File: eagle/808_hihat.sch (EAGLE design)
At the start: 129 parts, among them IC1 TL072P, IC2 TL072P, U4 4584N

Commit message: redoing board by hand from schematic
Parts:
- removed TM1*1, TM2*1: 220KB, TR808clone:TRIM_EU-CT6
- R44*1: value 150K -> 300K
- R45*1: value 100K -> 270K
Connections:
- removed net N$10: C5*1.2, TM2*1.E, U4E.I
- removed net N$11: C6*1.2, TM1*1.E, U4F.I
- net N$15: now also C5*1.2, U4E.I; no longer TM2*1.S
- net N$16: now also C6*1.2, U4F.I; no longer TM1*1.S
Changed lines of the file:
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@@
 <part name="R42*1" library="TR808clone" deviceset="R-EU_" device="0207/5V" value="680K"/>
 <part name="R43*1" library="TR808clone" deviceset="R-EU_" device="0207/5V" value="220K"/>
-<part name="R45*1" library="TR808clone" deviceset="R-EU_" device="0207/5V" value="100K"/>
+<part name="R45*1" library="TR808clone" deviceset="R-EU_" device="0207/5V" value="270K"/>
 <part name="C1*1" library="TR808clone" deviceset="C-EU" device="4MM_PITCH" value="18n"/>
 <part name="C2*1" library="TR808clone" deviceset="C-EU" device="3.5MM_PITCH" value="10n"/>
@@
 <part name="V9" library="supply1" deviceset="GND" device=""/>
 <part name="V10" library="supply1" deviceset="GND" device=""/>
-<part name="TM2*1" library="TR808clone" deviceset="TRIM_EU-" device="CT6" value="220KB"/>
-<part name="TM1*1" library="TR808clone" deviceset="TRIM_EU-" device="CT6" value="220KB"/>
-<part name="R44*1" library="TR808clone" deviceset="R-EU_" device="0207/5V" value="150K"/>
+<part name="R44*1" library="TR808clone" deviceset="R-EU_" device="0207/5V" value="300K"/>
 <part name="V11" library="supply1" deviceset="GND" device=""/>
 <part name="IC1" library="linear" deviceset="TL072" device="P"/>
@@
 <instance part="V9" gate="1" x="-55.88" y="-40.64"/>
 <instance part="V10" gate="1" x="-55.88" y="-12.7"/>
-<instance part="TM2*1" gate="1" x="-50.8" y="-22.86" smashed="yes" rot="R90">
-<attribute name="NAME" x="-57.15" y="-18.669" size="1.778" layer="95" rot="R180"/>
-<attribute name="VALUE" x="-57.15" y="-21.59" size="1.778" layer="96" rot="R180"/>
-</instance>
-<instance part="TM1*1" gate="1" x="-53.34" y="7.62" smashed="yes" rot="R90">
-<attribute name="NAME" x="-59.69" y="11.811" size="1.778" layer="95" rot="R180"/>
-<attribute name="VALUE" x="-59.69" y="8.89" size="1.778" layer="96" rot="R180"/>
-</instance>
 <instance part="R44*1" gate="G$1" x="-40.64" y="12.7" smashed="yes" rot="MR180">
 <attribute name="NAME" x="-44.45" y="11.2014" size="1.778" layer="95" rot="MR180"/>
@@
 </segment>
 </net>
-<net name="N$10" class="0">
-<segment>
-<pinref part="U4" gate="E" pin="I"/>
-<pinref part="C5*1" gate="G$1" pin="2"/>
-<wire x1="-55.88" y1="-30.48" x2="-55.88" y2="-22.86" width="0.1524" layer="91"/>
-<pinref part="TM2*1" gate="1" pin="E"/>
-<junction x="-55.88" y="-30.48"/>
-</segment>
-</net>
-<net name="N$11" class="0">
-<segment>
-<pinref part="U4" gate="F" pin="I"/>
-<pinref part="C6*1" gate="G$1" pin="2"/>
-<pinref part="TM1*1" gate="1" pin="E"/>
-<wire x1="-58.42" y1="7.62" x2="-58.42" y2="-2.54" width="0.1524" layer="91"/>
-<wire x1="-58.42" y1="-2.54" x2="-55.88" y2="-2.54" width="0.1524" layer="91"/>
-<junction x="-55.88" y="-2.54"/>
-</segment>
-</net>
 <net name="N$12" class="0">
 <segment>
@@
 <net name="N$15" class="0">
 <segment>
-<pinref part="TM2*1" gate="1" pin="S"/>
 <pinref part="R45*1" gate="G$1" pin="1"/>
-<wire x1="-50.8" y1="-17.78" x2="-45.72" y2="-17.78" width="0.1524" layer="91"/>
+<pinref part="U4" gate="E" pin="I"/>
+<pinref part="C5*1" gate="G$1" pin="2"/>
+<wire x1="-55.88" y1="-30.48" x2="-55.88" y2="-17.78" width="0.1524" layer="91"/>
+<junction x="-55.88" y="-30.48"/>
+<wire x1="-45.72" y1="-17.78" x2="-55.88" y2="-17.78" width="0.1524" layer="91"/>
 </segment>
 </net>
 <net name="N$16" class="0">
 <segment>
-<pinref part="TM1*1" gate="1" pin="S"/>
 <pinref part="R44*1" gate="G$1" pin="1"/>
-<wire x1="-53.34" y1="12.7" x2="-45.72" y2="12.7" width="0.1524" layer="91"/>
-</segment>
-</net>
+<wire x1="-58.42" y1="12.7" x2="-45.72" y2="12.7" width="0.1524" layer="91"/>
+<pinref part="U4" gate="F" pin="I"/>
+<pinref part="C6*1" gate="G$1" pin="2"/>
+<wire x1="-58.42" y1="12.7" x2="-58.42" y2="-2.54" width="0.1524" layer="91"/>
+<wire x1="-58.42" y1="-2.54" x2="-55.88" y2="-2.54" width="0.1524" layer="91"/>
+<junction x="-55.88" y="-2.54"/>
+</segment>
+</net>

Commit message: three routes left
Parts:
- R153*: device TR808clone:R-EU_0207/2V -> rcl:R-US_0207/5V
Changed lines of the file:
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@@
 <part name="C73*" library="TR808clone" deviceset="C-EU" device="3.5MM_PITCH" value="1n"/>
 <part name="R147*" library="TR808clone" deviceset="R-EU_" device="0207/2V" value="2K7"/>
-<part name="R153*" library="TR808clone" deviceset="R-EU_" device="0207/2V" value="2K7"/>
+<part name="R153*" library="rcl" deviceset="R-US_" device="0207/5V" value="2K7"/>
 <part name="R146*" library="TR808clone" deviceset="R-EU_" device="0207/5V" value="68K"/>
 <part name="R155*" library="TR808clone" deviceset="R-EU_" device="0207/5V" value="68K"/>

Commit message: routed but rough
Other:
- note added: "Hi-Hats"
- note removed: "HitHat"
- moved on the sheet: R44*1
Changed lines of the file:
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@@
 <description>HitHat</description>
 <plain>
-<text x="2.54" y="106.68" size="3.81" layer="94">HitHat</text>
+<text x="2.54" y="106.68" size="3.81" layer="94">Hi-Hats</text>
 </plain>
 <instances>
@@
 <instance part="V9" gate="1" x="-55.88" y="-40.64"/>
 <instance part="V10" gate="1" x="-55.88" y="-12.7"/>
-<instance part="R44*1" gate="G$1" x="-40.64" y="12.7" smashed="yes" rot="MR180">
-<attribute name="NAME" x="-44.45" y="11.2014" size="1.778" layer="95" rot="MR180"/>
-<attribute name="VALUE" x="-44.45" y="8.382" size="1.778" layer="96" rot="MR180"/>
+<instance part="R44*1" gate="G$1" x="-40.64" y="15.24" smashed="yes" rot="MR180">
+<attribute name="NAME" x="-44.45" y="13.7414" size="1.778" layer="95" rot="MR180"/>
+<attribute name="VALUE" x="-44.45" y="10.922" size="1.778" layer="96" rot="MR180"/>
 </instance>
 <instance part="V11" gate="1" x="-45.72" y="-12.7"/>
@@
 <instance part="IC1" gate="B" x="147.32" y="7.62" rot="MR180"/>
 <instance part="IC2" gate="A" x="7.62" y="-68.58" rot="MR180"/>
-<instance part="P+3" gate="1" x="-45.72" y="20.32"/>
+<instance part="P+3" gate="1" x="-45.72" y="10.16"/>
 <instance part="CH_ACCENT" gate="1" x="-106.68" y="114.3"/>
 <instance part="CH_TRIG" gate="1" x="-139.7" y="111.76"/>
@@
 <wire x1="-35.56" y1="-2.54" x2="-33.02" y2="-2.54" width="0.1524" layer="91"/>
 <pinref part="R44*1" gate="G$1" pin="2"/>
-<wire x1="-35.56" y1="12.7" x2="-35.56" y2="-2.54" width="0.1524" layer="91"/>
+<wire x1="-35.56" y1="15.24" x2="-35.56" y2="-2.54" width="0.1524" layer="91"/>
 <junction x="-35.56" y="-2.54"/>
 </segment>
@@
 <segment>
 <pinref part="R44*1" gate="G$1" pin="1"/>
-<wire x1="-58.42" y1="12.7" x2="-45.72" y2="12.7" width="0.1524" layer="91"/>
+<wire x1="-58.42" y1="12.7" x2="-45.72" y2="15.24" width="0.1524" layer="91"/>
 <pinref part="U4" gate="F" pin="I"/>
 <pinref part="C6*1" gate="G$1" pin="2"/>
@@
 <segment>
 <pinref part="U4" gate="P" pin="VDD"/>
-<wire x1="-45.72" y1="5.08" x2="-45.72" y2="17.78" width="0.1524" layer="91"/>
+<wire x1="-45.72" y1="5.08" x2="-45.72" y2="7.62" width="0.1524" layer="91"/>
 <pinref part="P+3" gate="1" pin="+5V"/>
 </segment>

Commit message: labeled the transistor values
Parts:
- Q21*, Q22*, Q23*, Q24*, Q26*, Q27*, Q28*, Q29*, Q3*, Q30*, Q31*, Q4*: value (none) -> BC546
- Q7*, Q8*: value (none) -> BC556
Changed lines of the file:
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@@
 </classes>
 <parts>
-<part name="Q4*" library="transistor" deviceset="*-NPN-" device="TO92-CBE" technology="BC546"/>
-<part name="Q8*" library="transistor" deviceset="*-PNP-" device="TO92-EBC" technology="BC556A"/>
+<part name="Q4*" library="transistor" deviceset="*-NPN-" device="TO92-CBE" technology="BC546" value="BC546"/>
+<part name="Q8*" library="transistor" deviceset="*-PNP-" device="TO92-EBC" technology="BC556A" value="BC556"/>
 <part name="R7*" library="TR808clone" deviceset="R-EU_" device="0207/5V" value="10K"/>
 <part name="R11*" library="TR808clone" deviceset="R-EU_" device="0207/5V" value="22K"/>
@@
 <part name="V358" library="supply1" deviceset="GND" device=""/>
 <part name="V359" library="supply1" deviceset="GND" device=""/>
-<part name="Q3*" library="transistor" deviceset="*-NPN-" device="TO92-CBE" technology="BC546"/>
-<part name="Q7*" library="transistor" deviceset="*-PNP-" device="TO92-EBC" technology="BC556A"/>
+<part name="Q3*" library="transistor" deviceset="*-NPN-" device="TO92-CBE" technology="BC546" value="BC546"/>
+<part name="Q7*" library="transistor" deviceset="*-PNP-" device="TO92-EBC" technology="BC556A" value="BC556"/>
 <part name="R8*" library="TR808clone" deviceset="R-EU_" device="0207/5V" value="10K"/>
 <part name="R12*" library="TR808clone" deviceset="R-EU_" device="0207/5V" value="22K"/>
@@
 <part name="V363" library="supply1" deviceset="GND" device=""/>
 <part name="R130*" library="TR808clone" deviceset="R-EU_" device="0207/5V" value="10K"/>
-<part name="Q21*" library="transistor" deviceset="*-NPN-" device="TO92-CBE" technology="BC546"/>
+<part name="Q21*" library="transistor" deviceset="*-NPN-" device="TO92-CBE" technology="BC546" value="BC546"/>
 <part name="V364" library="supply1" deviceset="GND" device=""/>
 <part name="C60*" library="TR808clone" deviceset="CPOL-EU" device="E2.5-5" value="10/16"/>
 <part name="V365" library="supply1" deviceset="GND" device=""/>
 <part name="R133*" library="TR808clone" deviceset="R-EU_" device="0207/5V" value="10K"/>
-<part name="Q22*" library="transistor" deviceset="*-NPN-" device="TO92-CBE" technology="BC546"/>
-<part name="Q23*" library="transistor" deviceset="*-NPN-" device="TO92-CBE" technology="BC546"/>
+<part name="Q22*" library="transistor" deviceset="*-NPN-" device="TO92-CBE" technology="BC546" value="BC546"/>
+<part name="Q23*" library="transistor" deviceset="*-NPN-" device="TO92-CBE" technology="BC546" value="BC546"/>
 <part name="R134*" library="TR808clone" deviceset="R-EU_" device="0207/5V" value="100K"/>
 <part name="R135*" library="TR808clone" deviceset="R-EU_" device="0207/5V" value="10K"/>
-<part name="Q24*" library="transistor" deviceset="*-NPN-" device="TO92-CBE" technology="BC546"/>
+<part name="Q24*" library="transistor" deviceset="*-NPN-" device="TO92-CBE" technology="BC546" value="BC546"/>
 <part name="R137*" library="TR808clone" deviceset="R-EU_" device="0207/5V" value="470R"/>
 <part name="C62*" library="TR808clone" deviceset="CPOL-EU" device="E2.5-5" value=".47/50"/>
@@
 <part name="C61*" library="TR808clone" deviceset="CPOL-EU" device="E2.5-5" value="47/16"/>
 <part name="V370" library="supply1" deviceset="GND" device=""/>
-<part name="Q29*" library="transistor" deviceset="*-NPN-" device="TO92-CBE" technology="BC546"/>
+<part name="Q29*" library="transistor" deviceset="*-NPN-" device="TO92-CBE" technology="BC546" value="BC546"/>
 <part name="R143*" library="TR808clone" deviceset="R-EU_" device="0207/5V" value="33K"/>
 <part name="V371" library="supply1" deviceset="GND" device=""/>
 <part name="R136*" library="TR808clone" deviceset="R-EU_" device="0207/5V" value="100R"/>
-<part name="Q28*" library="transistor" deviceset="*-NPN-" device="TO92-CBE" technology="BC546"/>
+<part name="Q28*" library="transistor" deviceset="*-NPN-" device="TO92-CBE" technology="BC546" value="BC546"/>
 <part name="R141*" library="TR808clone" deviceset="R-EU_" device="0207/5V" value="33K"/>
 <part name="R173*" library="TR808clone" deviceset="R-EU_" device="0207/5V" value="330K"/>
 <part name="C63*" library="TR808clone" deviceset="CPOL-EU" device="E2.5-5" value=".47/50"/>
 <part name="V374" library="supply1" deviceset="GND" device=""/>
-<part name="Q27*" library="transistor" deviceset="*-NPN-" device="TO92-CBE" technology="BC546"/>
+<part name="Q27*" library="transistor" deviceset="*-NPN-" device="TO92-CBE" technology="BC546" value="BC546"/>
 <part name="C67*" library="TR808clone" deviceset="C-EU" device="4MM_PITCH" value="22n"/>
-<part name="Q30*" library="transistor" deviceset="*-NPN-" device="TO92-CBE" technology="BC546"/>
+<part name="Q30*" library="transistor" deviceset="*-NPN-" device="TO92-CBE" technology="BC546" value="BC546"/>
 <part name="V375" library="supply1" deviceset="GND" device=""/>
 <part name="V376" library="supply1" deviceset="GND" device=""/>
@@
 <part name="V383" library="supply1" deviceset="GND" device=""/>
 <part name="V384" library="supply1" deviceset="GND" device=""/>
-<part name="Q26*" library="transistor" deviceset="*-NPN-" device="TO92-CBE" technology="BC546"/>
-<part name="Q31*" library="transistor" deviceset="*-NPN-" device="TO92-CBE" technology="BC546"/>
+<part name="Q26*" library="transistor" deviceset="*-NPN-" device="TO92-CBE" technology="BC546" value="BC546"/>
+<part name="Q31*" library="transistor" deviceset="*-NPN-" device="TO92-CBE" technology="BC546" value="BC546"/>
 <part name="C80*" library="TR808clone" deviceset="C-EU" device="3.5MM_PITCH" value="470p"/>
 <part name="C74*" library="TR808clone" deviceset="C-EU" device="3.5MM_PITCH" value="470p"/>

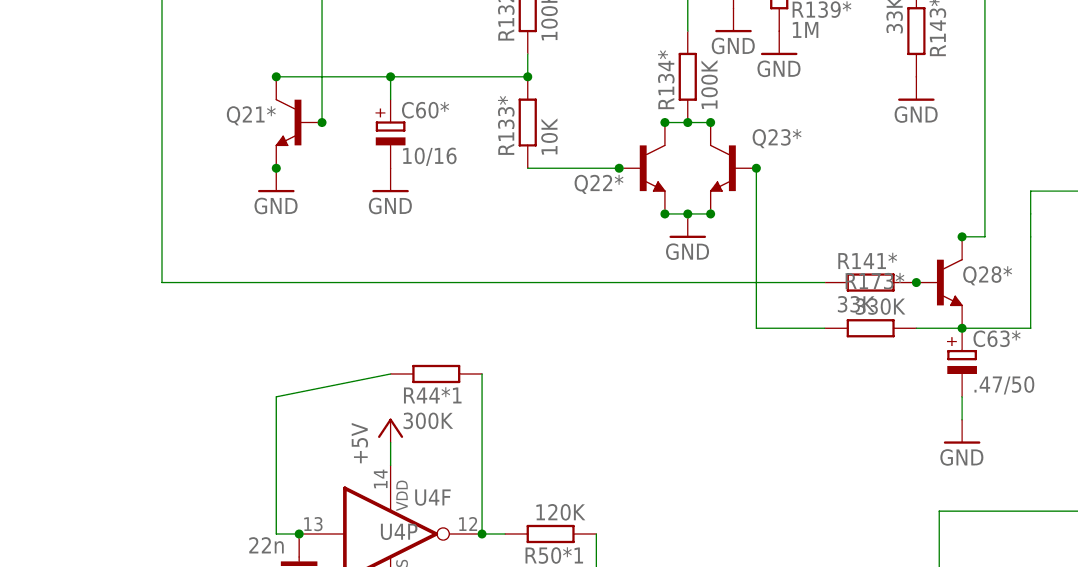
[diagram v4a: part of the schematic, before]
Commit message: ready for a test run on the cnc
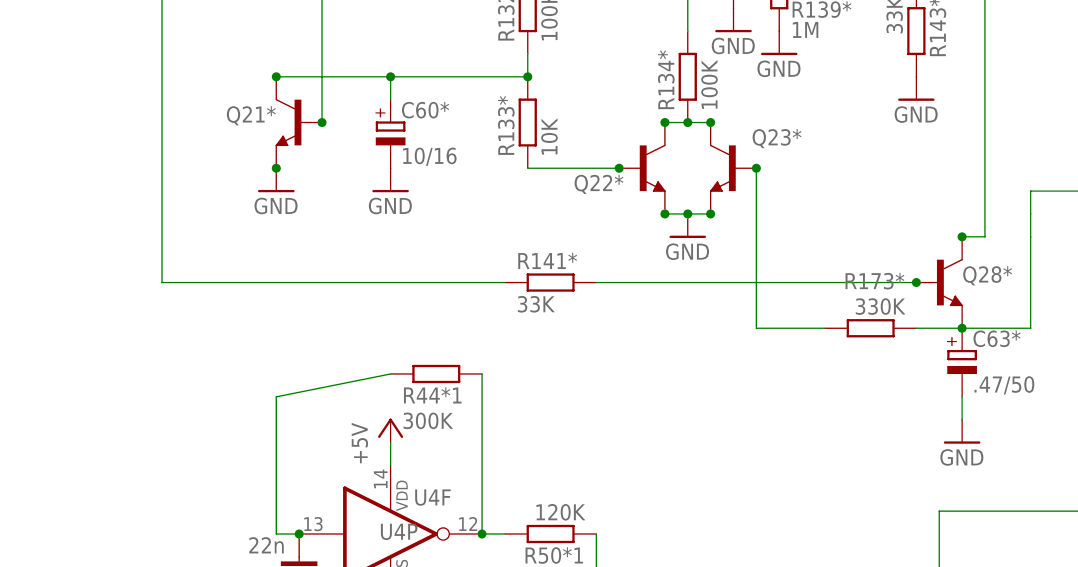
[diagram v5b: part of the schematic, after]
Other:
- moved on the sheet: R141*
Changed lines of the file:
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@@
 <attribute name="NAME" x="17.78" y="25.4" size="1.778" layer="95"/>
 </instance>
-<instance part="R141*" gate="G$1" x="7.62" y="25.4"/>
+<instance part="R141*" gate="G$1" x="-27.94" y="25.4"/>
 <instance part="R173*" gate="G$1" x="7.62" y="20.32" smashed="yes" rot="R180">
 <attribute name="NAME" x="11.43" y="26.4414" size="1.778" layer="95" rot="R180"/>
@@
 <wire x1="-99.06" y1="86.36" x2="-71.12" y2="86.36" width="0.1524" layer="91"/>
 <wire x1="-71.12" y1="86.36" x2="-71.12" y2="25.4" width="0.1524" layer="91"/>
-<wire x1="-71.12" y1="25.4" x2="2.54" y2="25.4" width="0.1524" layer="91"/>
+<wire x1="-71.12" y1="25.4" x2="-33.02" y2="25.4" width="0.1524" layer="91"/>
 <junction x="-99.06" y="86.36"/>
 <pinref part="R13*" gate="G$1" pin="2"/>
@@
 <pinref part="R141*" gate="G$1" pin="2"/>
 <pinref part="Q28*" gate="G$1" pin="B"/>
+<wire x1="-22.86" y1="25.4" x2="12.7" y2="25.4" width="0.1524" layer="91"/>
 <junction x="12.7" y="25.4"/>
 </segment>

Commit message: replaced parts
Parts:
- removed C1, C2, C3, C4: 22p, TR808clone:C-EU025-025X050
- removed C1*1, C4*1, C5*1: 18n, TR808clone:C-EU4MM_PITCH
- removed C2*1, C3*1: 10n, TR808clone:C-EU3.5MM_PITCH
- removed C5, C6: 0.1uF, TR808clone:C-EU3.5MM_PITCH
- removed C6*1: 22n, TR808clone:C-EU4MM_PITCH
- removed CH_OUT, OH_OUT: LSP11, solpad:LSP11
- removed D1, D2: 1N4148DO35-7, TR808clone:1N4148DO35-7
- removed Q21*, Q22*, Q23*, Q24*, Q26*, Q27*, Q28*, Q29*, Q3*, Q30*, Q31*, Q4*: BC546, transistor:BC546-NPN-TO92-CBE
- removed Q7*, Q8*: BC556, transistor:BC556A-PNP-TO92-EBC
- removed R1, R2: 22K, TR808clone:R-EU_0207/5V
- removed R35*1, R37*1, R39*1, R46*1, R48*1, R50*1: 120K, TR808clone:R-EU_0207/5V
- removed R40*1, R41*1: 560K, TR808clone:R-EU_0207/5V
- removed R42*1: 680K, TR808clone:R-EU_0207/5V
- removed R43*1: 220K, TR808clone:R-EU_0207/5V
- removed R44*1: 300K, TR808clone:R-EU_0207/5V
- removed R45*1: 270K, TR808clone:R-EU_0207/5V
- removed R53*1: 1K, TR808clone:R-EU_0207/5V
- removed U4: 4584N, TR808clone:4584N
- added CH_OUTPUT, OH_OUTPUT: AUDIO-JACK, erthenvar:AUDIO-JACK
- added CH_OUT_NORM, DIGI_NOISE, OH_OUT_NORM: 22-23-2021, con-molex:22-23-2021
- added Q1, Q10, Q11, Q12, Q2, Q3, Q4, Q5, Q6, Q7, Q8, Q9: 2N3904, 808_lt:2N3904
- added Q13, Q14: 2N3906, 808_lt:2N3906
- added U$2: POWER, eurorack:POWER
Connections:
- removed net N$12: R35*1.2, R40*1.1, U4C.O
- removed net N$13: R37*1.1, R41*1.2, U4B.O
- removed net N$14: R43*1.1, R46*1.2, U4D.O
- removed net N$15: C5*1.2, R45*1.1, U4E.I
- removed net N$16: C6*1.2, R44*1.1, U4F.I
- removed net N$19: R39*1.1, R42*1.1, U4A.O
- removed net N$22: C5.1, D1.C, R1.2
- removed net N$23: D1.A, OH_TRIG.MP
- removed net N$24: C6.1, D2.C, R2.2
- removed net N$26: CH_TRIG.MP, D2.A
- removed net N$27: IC2B.-IN, IC2B.OUT
- removed net N$583: Q30*.E, R152*.1
- removed net N$584: Q27*.E, R145*.1
- removed net N$606: Q29*.B, R140*.2
- removed net N$9: C4*1.2, R43*1.2, U4D.I
- removed net TP1: R45*1.2, R48*1.1, U4E.O
- removed net TP2: R44*1.2, R50*1.2, U4F.O
- new net N$10: OH_OUTPUT.NORM, OH_OUT_NORM-1.S
- new net N$11: CH_OUTPUT.NORM, CH_OUT_NORM-1.S
- net +12V: now also Q1.C, Q2.C, Q6.C, U$2.+12V; no longer C1.1, C2.2, IC1P.V+, IC2P.V+, Q26*.C, Q29*.C, Q31*.C
- net +5V: now also U$2.+5V; no longer U4P.VDD
- net -12V: now also U$2.-12V; no longer C3.2, C4.1, IC1P.V-, IC2P.V-
- net .: now also Q14.E, U$2.CV; no longer Q8*.E
- net CH_OUT: now also CH_OUTPUT.TIP; no longer CH_OUT.MP
- net GND: now also CH_OUTPUT.RING, CH_OUT_NORM-2.S, DIGI_NOISE-1.S, OH_OUTPUT.RING, OH_OUT_NORM-2.S, Q10.E, Q11.E, Q12.E, Q8.E, Q9.E, U$2.GND; no longer C1*1.1, C1.2, C2*1.1, C2.1, C3*1.1, C3.1, C4*1.1, C4.2, C5*1.1, C6*1.1, IC2B.+IN, Q21*.E, Q22*.E, Q23*.E, Q3*.E, Q4*.E, R1.1, R2.1, R53*1.1, U4P.VSS
- net N$17: now also Q13.E, U$1.CV; no longer Q7*.E
- net N$18: now also OH_TRIG.MP, U$1.GATE; no longer C5.2
- net N$2: now also DIGI_NOISE-2.S; no longer R35*1.1, R37*1.2, R39*1.2, R46*1.1, R48*1.2, R50*1.1, R53*1.2
- net N$25: now also CH_TRIG.MP, U$2.GATE; no longer C6.2
- net N$559: now also Q12.B; no longer Q4*.B
- net N$560: now also Q14.B; no longer Q8*.B
- net N$562: now also Q12.C; no longer Q4*.C
- net N$563: now also Q14.C; no longer Q8*.C
- net N$566: now also Q11.B; no longer Q3*.B
- net N$567: now also Q13.B; no longer Q7*.B
- net N$568: now also Q11.C; no longer Q3*.C
- net N$569: now also Q13.C; no longer Q7*.C
- net N$571: now also Q7.C; no longer Q24*.C
- net N$572: now also Q7.B; no longer Q24*.B
- net N$573: now also Q7.E; no longer Q24*.E
- net N$574: now also Q8.C, Q9.C; no longer Q22*.C, Q23*.C
- net N$575: now also Q8.B; no longer Q22*.B
- net N$576: now also Q10.C; no longer Q21*.C
- net N$578: now also Q5.B; no longer Q28*.B
- net N$579: now also Q5.C; no longer Q28*.C
- net N$580: now also Q9.B; no longer Q23*.B
- net N$581: now also Q5.E; no longer Q28*.E
- net N$582: now also Q6.E; no longer Q29*.E
- net N$585: now also Q3.B; no longer Q30*.B
- net N$586: now also Q4.B; no longer Q27*.B
- net N$587: now also Q3.C; no longer Q30*.C
- net N$588: now also Q4.C; no longer Q27*.C
- net N$591: now also Q1.B; no longer Q26*.B
- net N$592: now also Q2.B; no longer Q31*.B
- net N$6: now also Q6.B, R140*.2; no longer C1*1.2, R40*1.2, U4C.I
- net N$604: now also Q10.B; no longer Q21*.B
- net N$607: now also Q1.E; no longer Q26*.E
- net N$608: now also Q2.E; no longer Q31*.E
- net N$7: now also Q4.E, R145*.1; no longer C2*1.2, R41*1.1, U4B.I
- net N$8: now also Q3.E, R152*.1; no longer C3*1.2, R42*1.2, U4A.I
- net OH_OUT: now also OH_OUTPUT.TIP; no longer OH_OUT.MP
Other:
- moved on the sheet: C11*1, C15*1, C16*1, C63*, CH_ACCENT, CH_TRIG, IC2A, OH_TRIG, R11*, R13*, R145*, R157*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
